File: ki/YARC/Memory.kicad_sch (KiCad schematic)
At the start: 13 parts, among them U14 74LS20, U18 AS6C6264, U20 74HC00, U21 74LS08, U22 74LS139, U23 74LS32, U24 AS6C6264, U25 74HC245, U26 74LS157, U27 AS6C6264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

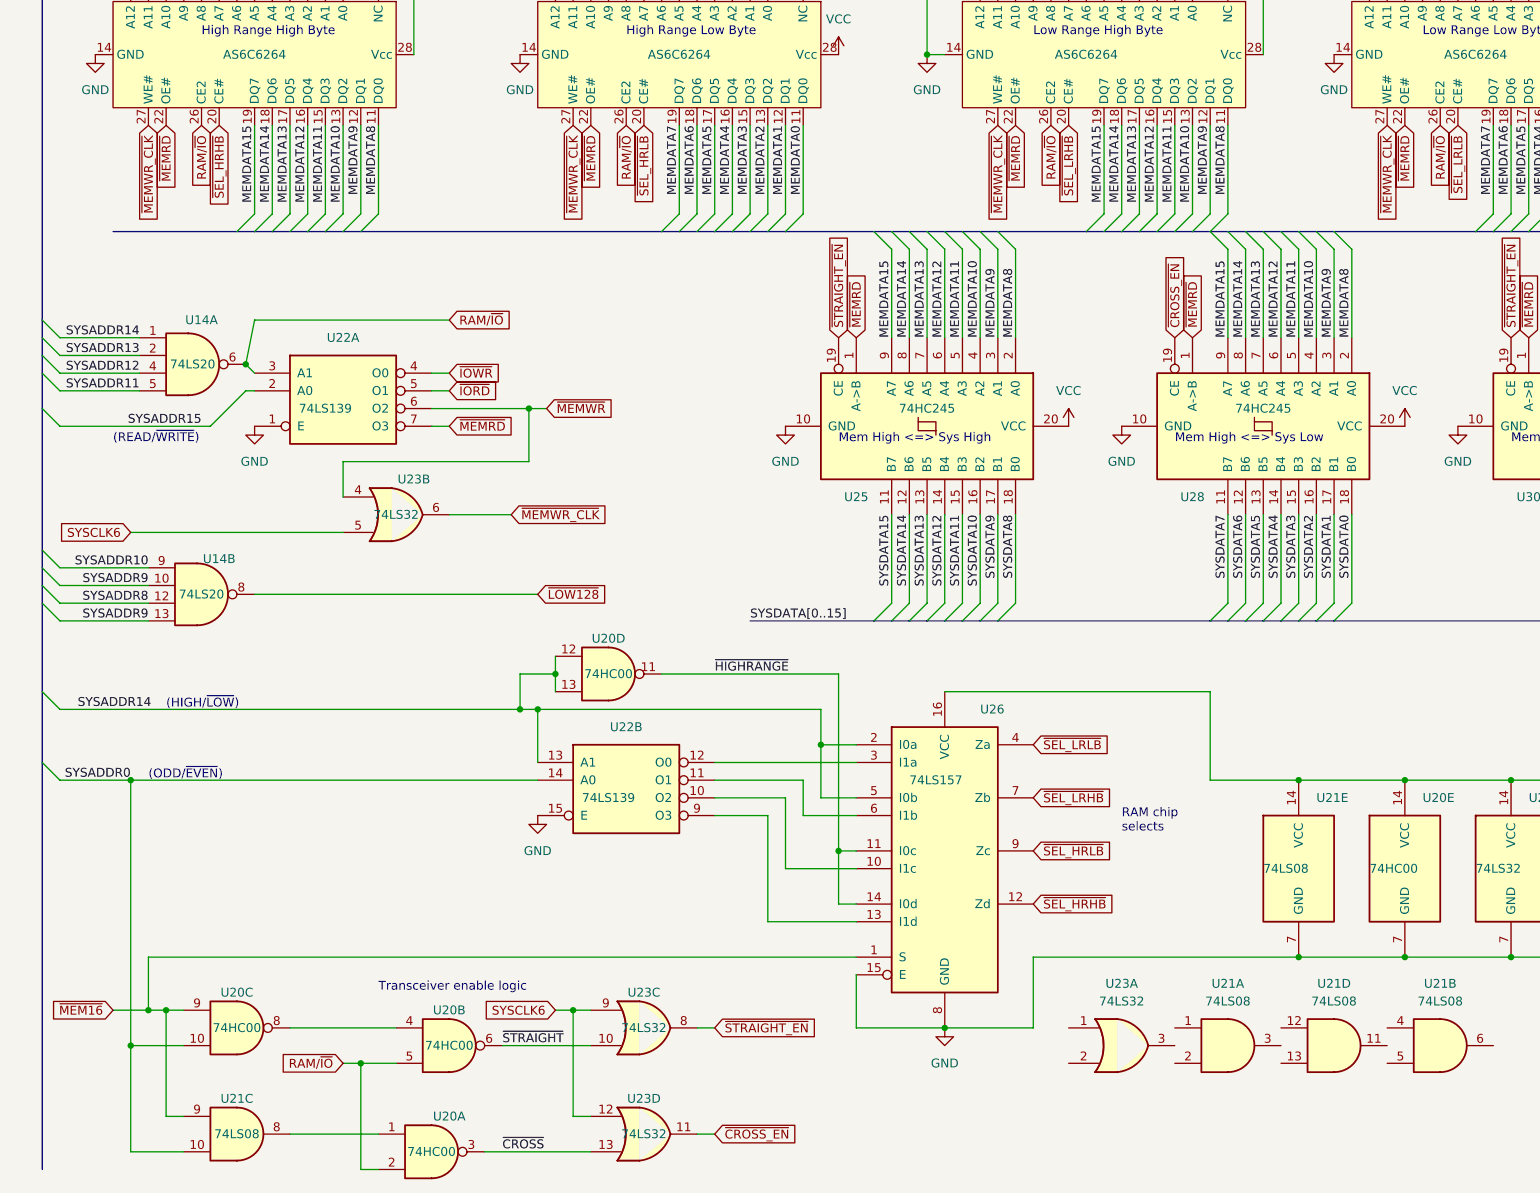
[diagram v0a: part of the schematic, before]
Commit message: Add some memory documentation and revise memory read logic
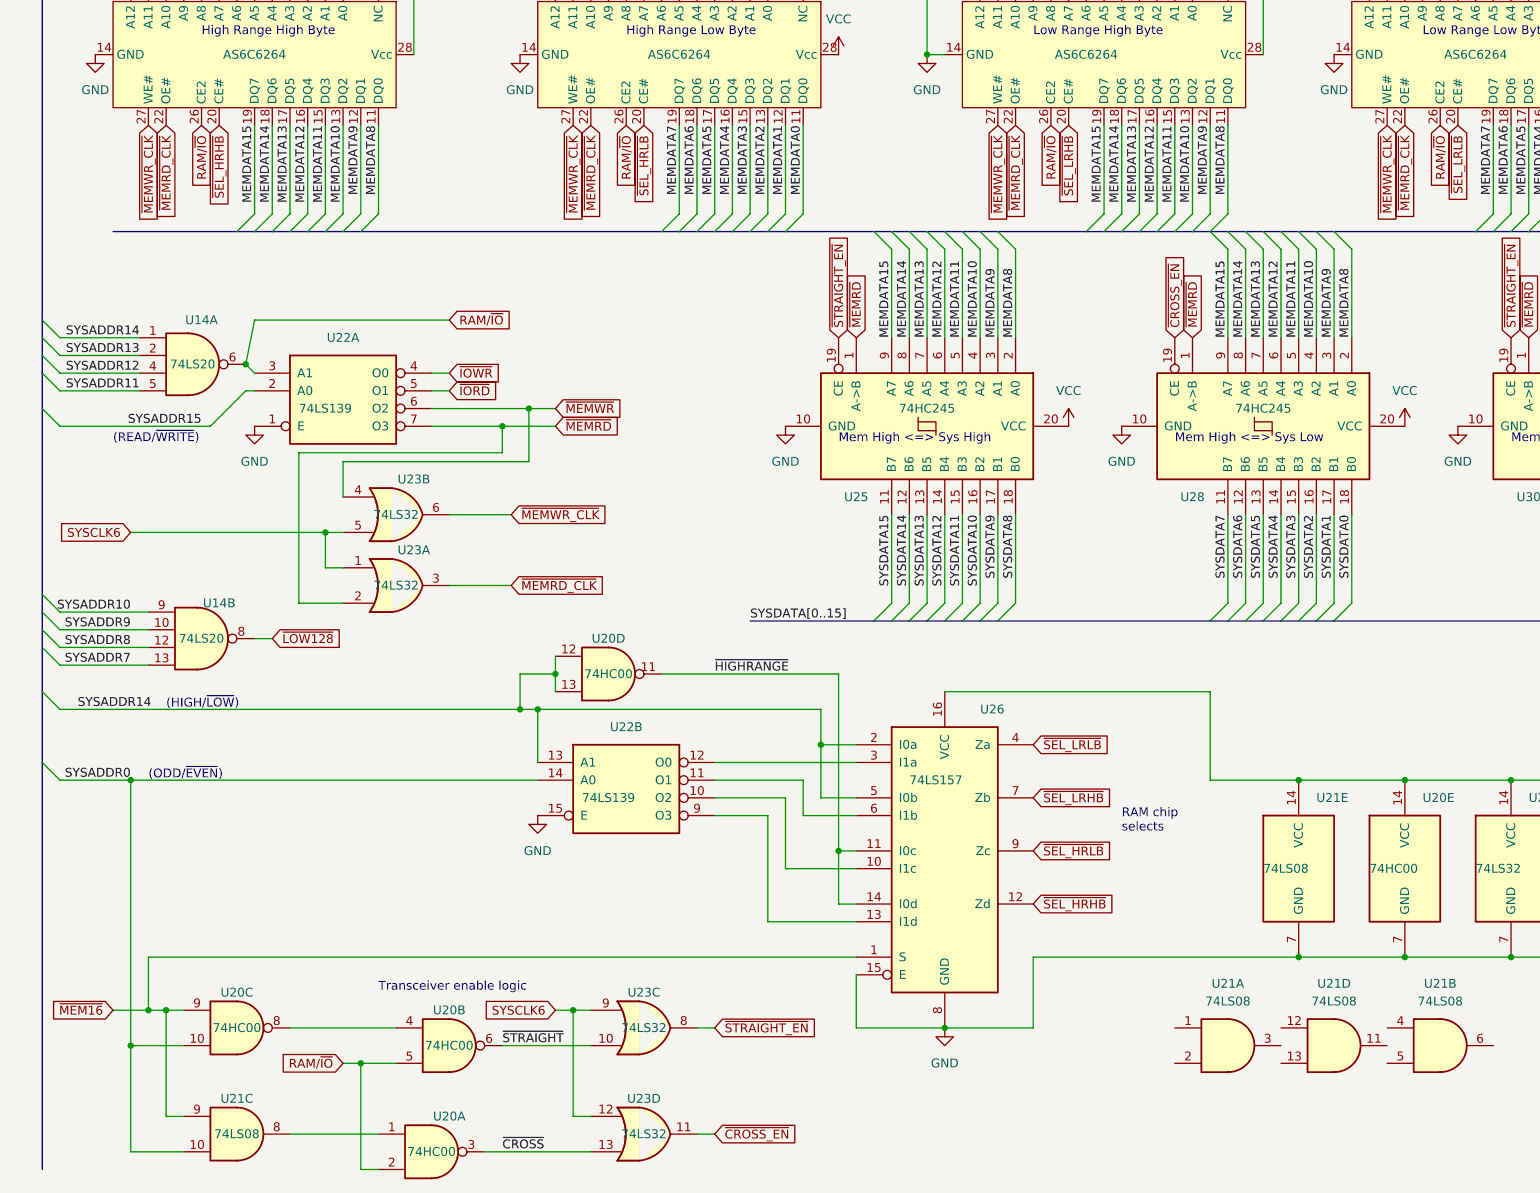
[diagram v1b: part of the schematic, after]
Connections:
- net SYSADDR7: now also U14.13
- net SYSADDR9: no longer U14.13
- net SYSCLK6: now also U23.1
- net ~{MEMRD}: now also U23.2; no longer U18.22 (OE#), U24.22 (OE#), U27.22 (OE#), U29.22 (OE#)
- net ~{MEMRD_CLK}: now reaches U23.3
- net ~{MEMRD_CLK}: now also U18.22 (OE#), U24.22 (OE#), U27.22 (OE#), U29.22 (OE#)
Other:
- moved on the sheet: U14B, U23A

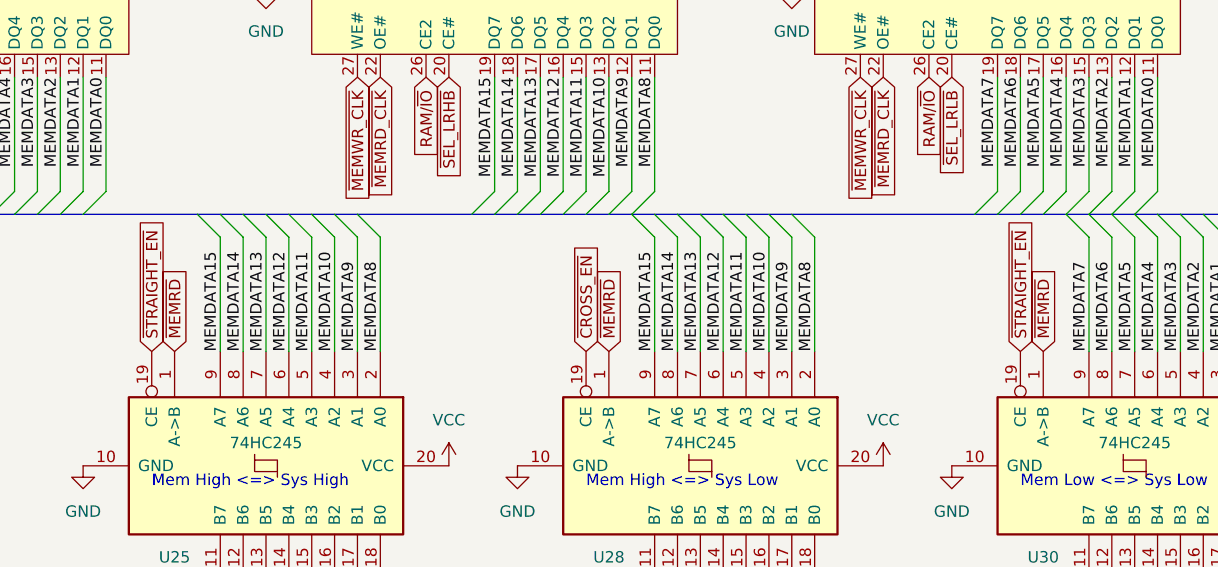
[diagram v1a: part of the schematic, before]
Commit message: Add gitignore. Update memory read signal. Update memory transceiver direction control. Many routing improvements.
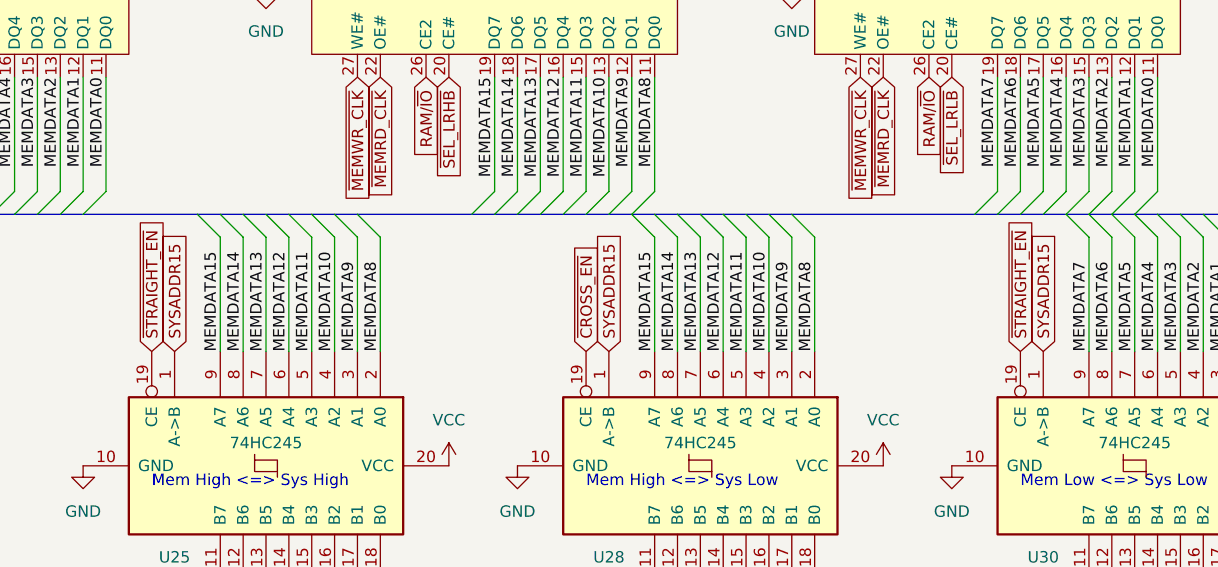
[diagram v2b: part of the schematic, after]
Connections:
- net SYSADDR15: now also U25.1 (A->B), U28.1 (A->B), U30.1 (A->B)
- net ~{MEMRD}: no longer U25.1 (A->B), U28.1 (A->B), U30.1 (A->B)
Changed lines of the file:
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@@
     )
   )
-  (global_label "~{MEMRD}" (shape input) (at 132.08 81.28 90) (fields_autoplaced)
+  (global_label "SYSADDR15" (shape input) (at 132.08 81.28 90) (fields_autoplaced)
     (effects (font (size 1.27 1.27)) (justify left))
-    (property "Intersheet References" "${INTERSHEET_REFS}" (id 0) (at 132.0006 72.275 90)
+    (property "Intersheet References" "${INTERSHEET_REFS}" (id 0) (at 132.0006 68.0417 90)
       (effects (font (size 1.27 1.27)) (justify left) hide)
     )
@@
     )
   )
-  (global_label "~{MEMRD}" (shape input) (at 228.6 81.28 90) (fields_autoplaced)
+  (global_label "SYSADDR15" (shape input) (at 228.6 81.28 90) (fields_autoplaced)
     (effects (font (size 1.27 1.27)) (justify left))
-    (property "Intersheet References" "${INTERSHEET_REFS}" (id 0) (at 228.5206 72.275 90)
+    (property "Intersheet References" "${INTERSHEET_REFS}" (id 0) (at 228.5206 68.0417 90)
       (effects (font (size 1.27 1.27)) (justify left) hide)
     )
@@
     )
   )
-  (global_label "~{MEMRD}" (shape input) (at 180.34 81.28 90) (fields_autoplaced)
+  (global_label "SYSADDR15" (shape input) (at 180.34 81.28 90) (fields_autoplaced)
     (effects (font (size 1.27 1.27)) (justify left))
-    (property "Intersheet References" "${INTERSHEET_REFS}" (id 0) (at 180.2606 72.275 90)
+    (property "Intersheet References" "${INTERSHEET_REFS}" (id 0) (at 180.2606 68.0417 90)
       (effects (font (size 1.27 1.27)) (justify left) hide)
     )

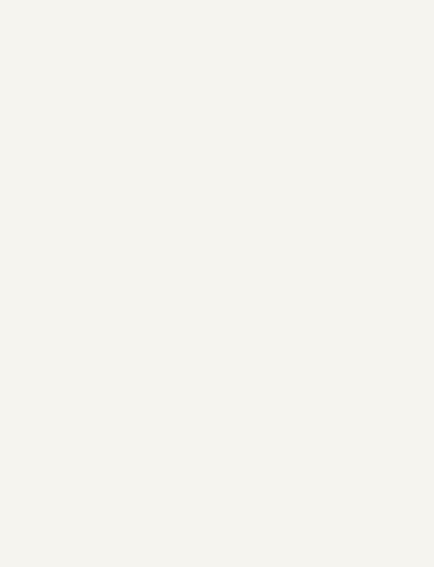
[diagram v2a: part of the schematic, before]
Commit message: Add microcode engine to KiCad. Minor updates to README.
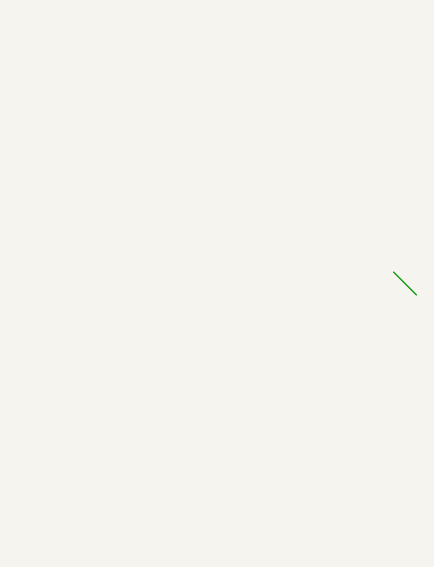
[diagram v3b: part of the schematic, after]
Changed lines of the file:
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@@
+    (stroke (width 0) (type default) (color 0 0 0 0))
+  )
+  (bus_entry (at 400.05 69.85) (size 2.54 2.54)
     (stroke (width 0) (type default) (color 0 0 0 0))
   )

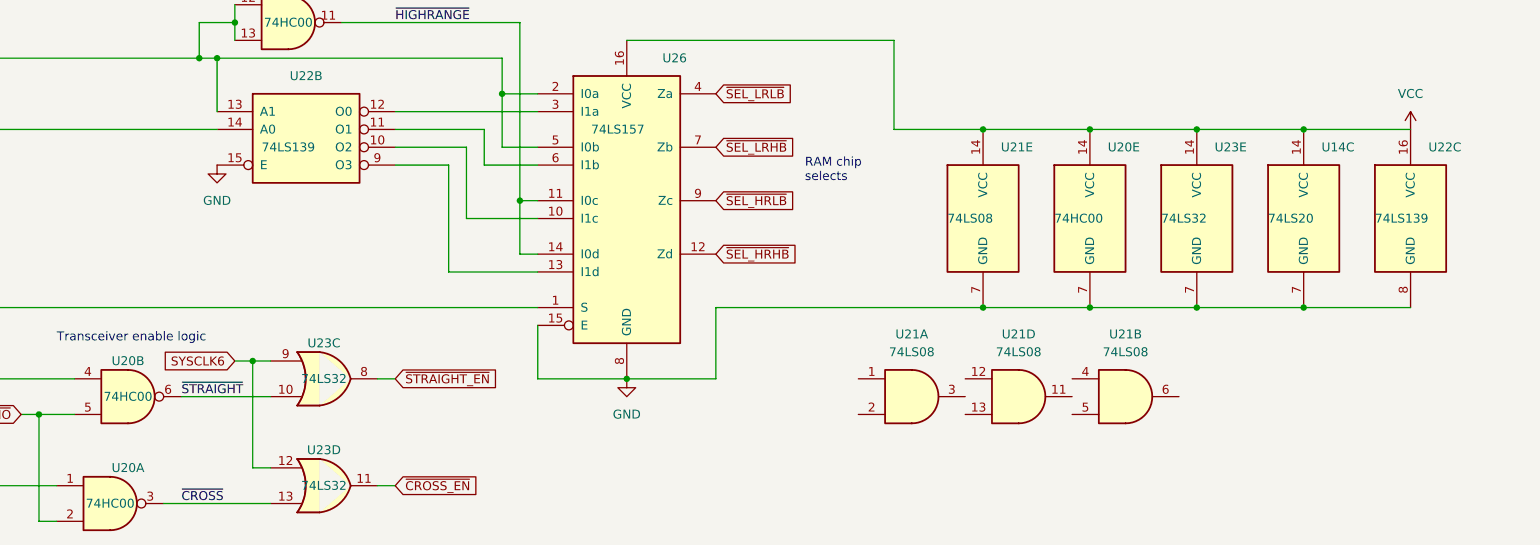
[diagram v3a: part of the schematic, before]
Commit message: Add MEM_EN# fix to arch.yasm, KiCad, and Fritzing
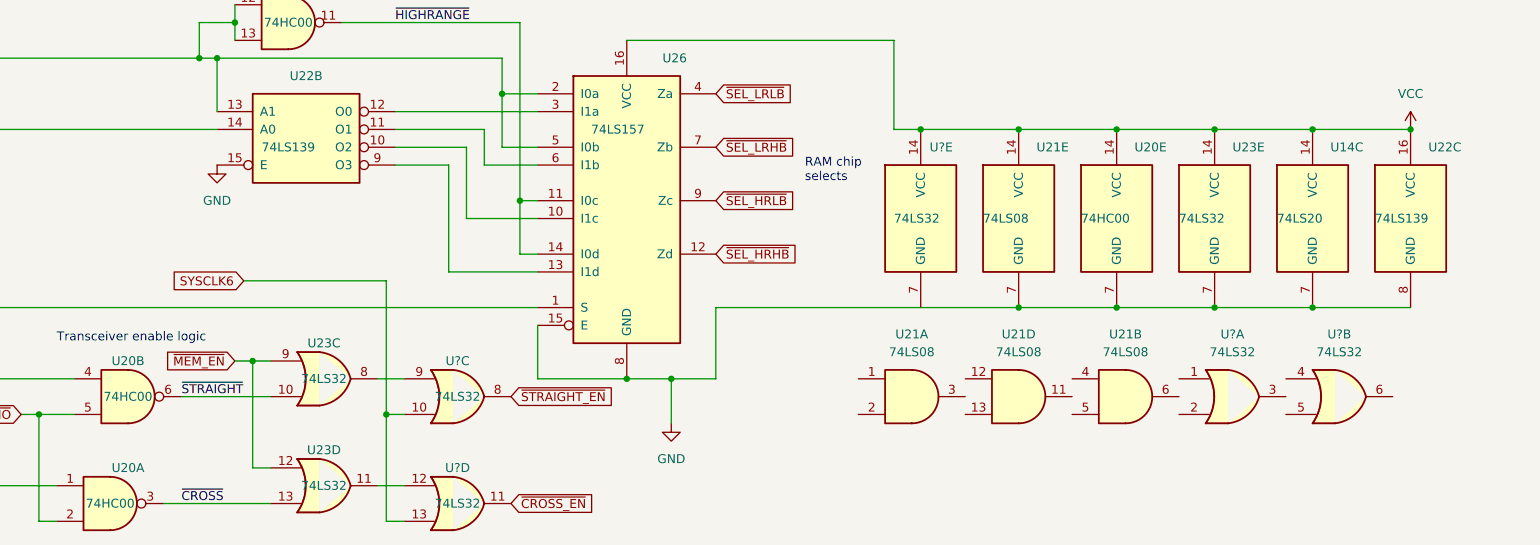
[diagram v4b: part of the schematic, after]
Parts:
- added U? (x5): 74LS32, symbol 74xx:74LS32
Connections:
- net SYSCLK6: now also U?.10, U?.13; no longer U23.12, U23.9
- net VCC: now also U?.14 (VCC)
- net ~{CROSS_EN}: now also U?.11; no longer U23.11
- net ~{STRAIGHT_EN}: now also U?.8; no longer U23.8
- new net: U23.8, U?.9
- new net: U23.11, U?.12
- new net ~{MEM_EN}: U23.12, U23.9
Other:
- moved on the sheet: U14C, U20E, U21E, U23E
